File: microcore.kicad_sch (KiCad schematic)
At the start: 5 parts, among them J1 TE_776231-1, J8 USB_B_Mini, M1 Module:mega-mcu100/0.3, M2 Module-power_12and5V-0.3, M3 Module-vr-max9924-0.3

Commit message: Fix top schematic wiring so labels connect to Hellen module pins
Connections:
- net AN1: now also J1.19, M1.S9 (IN_AUX1_(PB0))
- net AN2: now also J1.21, M1.S8 (IN_AUX2_(PC4/PE9))
- net CAN_H: now also J1.2, M1.W11 (CANH)
- net CAN_L: now also J1.3, M1.W12 (CANL)
- net CLT: now also J1.24 (16), M1.S21 (IN_CLT_(PC2))
- net GND: now also J1.22, J1.23, J8.5 (GND), J8.6 (Shield), M1.G (GND), M2.S1 (GND), M3.G (GND)
- net HALL_CAM: now also J1.27 (17), M1.S16 (IN_CAM_(PA6))
- net IAT: now also J1.25 (17), M1.S20 (IN_IAT_(PC3))
- net IGN1: now also J1.12
- net IGN2: now also J1.13, M1.W9 (IGN2_(PE5))
- net IGN3: now also J1.14, M1.W8 (IGN3_(PE4))
- net IGN4: now also J1.15, M1.W7 (IGN4_(PE3))
- net INJ1: now also J1.4
- net INJ2: now also J1.5
- net INJ3: now also J1.6
- net INJ4: now also J1.7
- net LS1_FP: now also J1.8
- net LS2_IDLE: now also J1.9
- net LS3_BOOST: now also J1.10
- net MAP: now also J1.18, M1.S13 (IN_MAP1_(PC0))
- net OUT_INJ1: now also M1.E17 (OUT_INJ1_(PD3))
- net OUT_INJ2: now also M1.E16 (OUT_INJ2_(PA9))
- net OUT_INJ3: now also M1.E15 (OUT_INJ3_(PD11))
- net OUT_INJ4: now also M1.E14 (OUT_INJ4_(PD10))
- net OUT_LS1: now also M1.E18 (OUT_PWM1_(PD13))
- net OUT_LS2: now also M1.E19 (OUT_PWM2_(PC6))
- net OUT_LS3: now also M1.E20 (OUT_PWM3_(PC7))
- net SGND: now also J1.20, M1.E2 (GNDA), M1.W1 (GNDA)
- net TPS: now also J1.17, M1.S18 (IN_TPS_(PA4))
- net USBID_(PA10): now also J8.4 (ID), M1.N4 (USBID_(PA10)); no longer J8.1 (VBUS)
- net USBM_(PA11): now also J8.2 (D-), M1.N2 (USBM_(PA11))
- net USBP_(PA12): now also M1.N3 (USBP_(PA12))
- net V12_RAW: now also M2.V3 (V12_RAW)
- net V5_REF: now also J1.16, M2.E4 (V5), M3.E4 (V5_IN)
- net VBAT: now also M1.N17 (VBAT), M2.E1 (VBAT)
- net VBUS: now also J8.1 (VBUS), M1.N1 (VBUS); no longer J8.4 (ID)
- net VIGN: now also M2.E3 (VIGN)
- net VIGN_SENSE: now also M1.E5 (IN_VIGN_(PA5)), M2.V2 (IN_VIGN)
- net VR_N: now also J1.29 (17), M3.W1 (VR-/HALL)
- net VR_OUT: now also M1.S14 (IN_CRANK_(PB1)), M3.E3 (OUT)
- net VR_P: now also J1.28 (16), M3.W2 (VR+)
- no-connect marks 0 -> 8
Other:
- moved on the sheet: J8

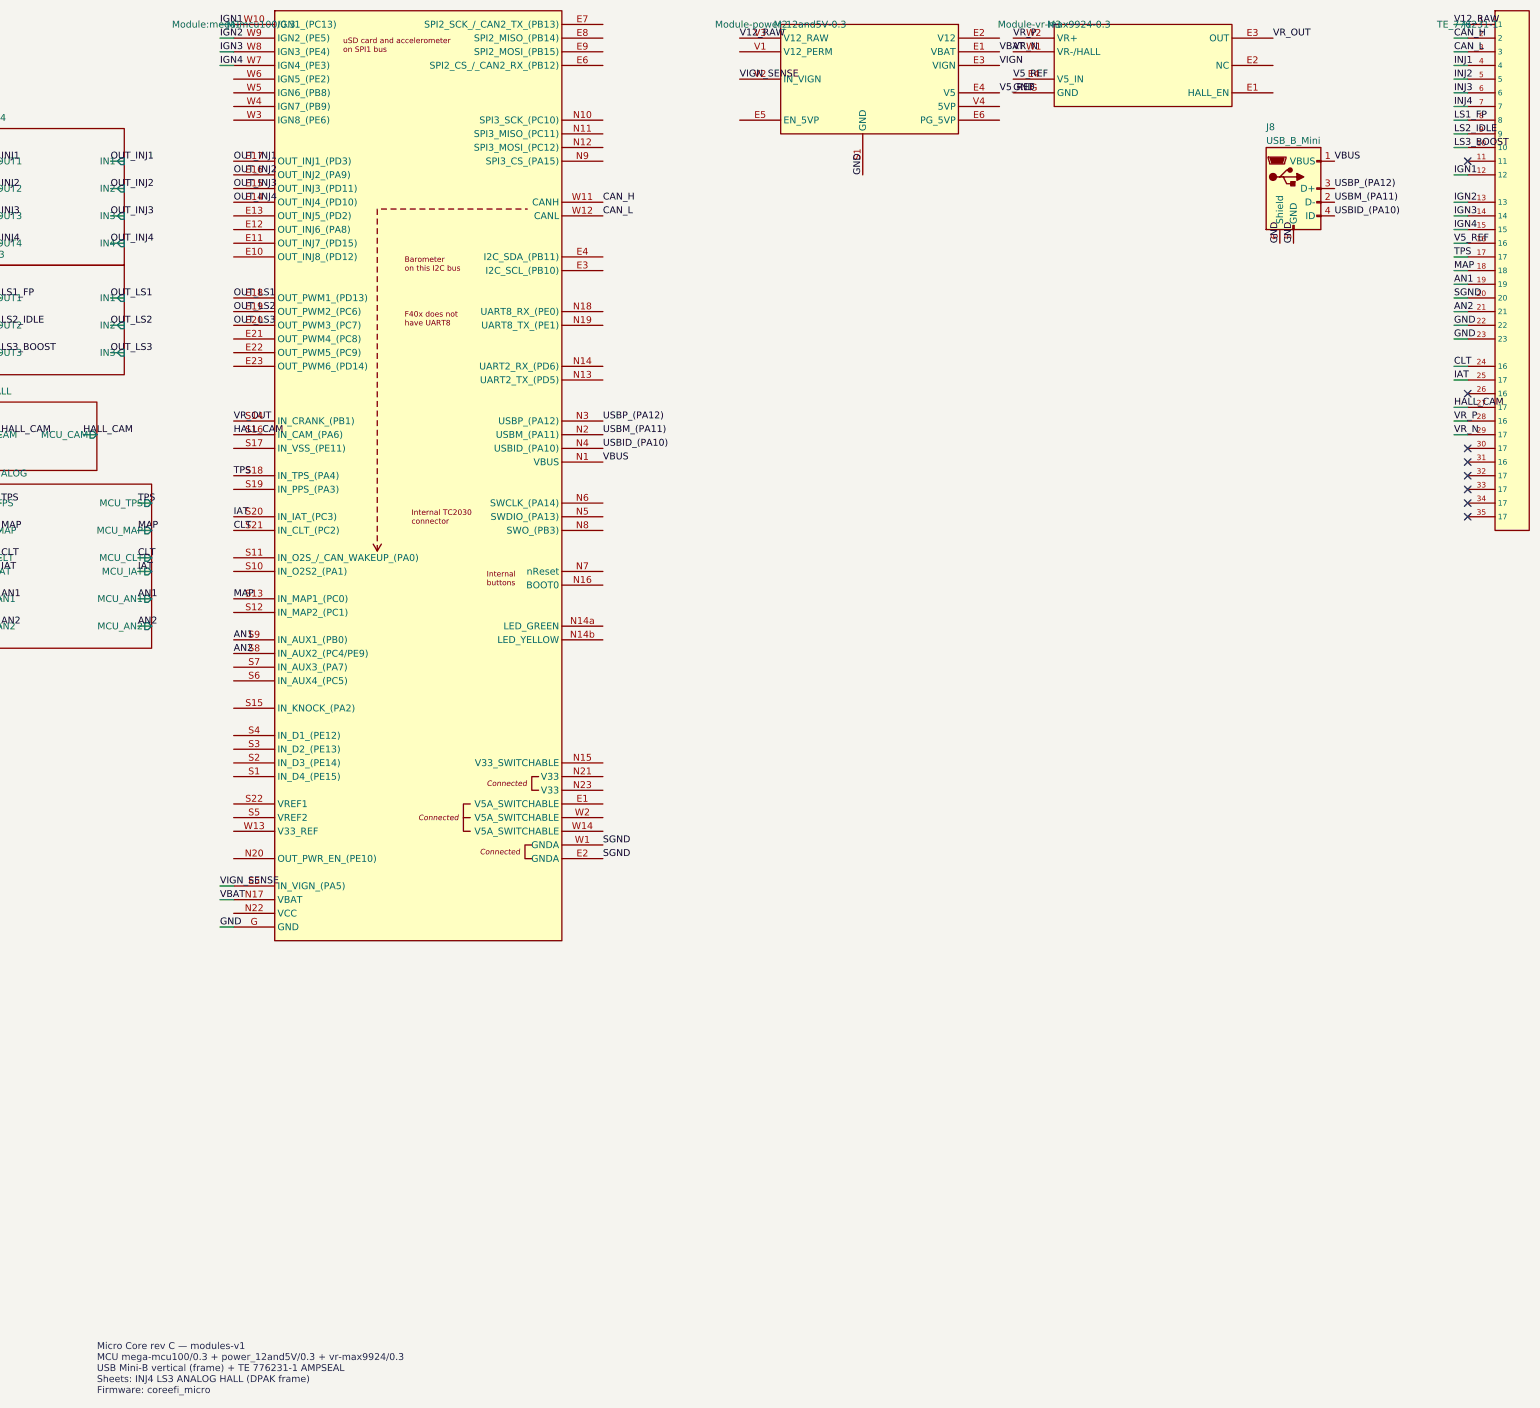
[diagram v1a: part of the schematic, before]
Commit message: Freeze AMPSEAL spare pins and add frame BOOT/RESET (rev d)
Assign pins 11/26/30–35 to DIN1–2, IGN5–8, SGND, PGND; wire to mega.
Add gasketed SW_BOOT (BOOT0–V33) and SW_RESET (nReset–GND) near USB.
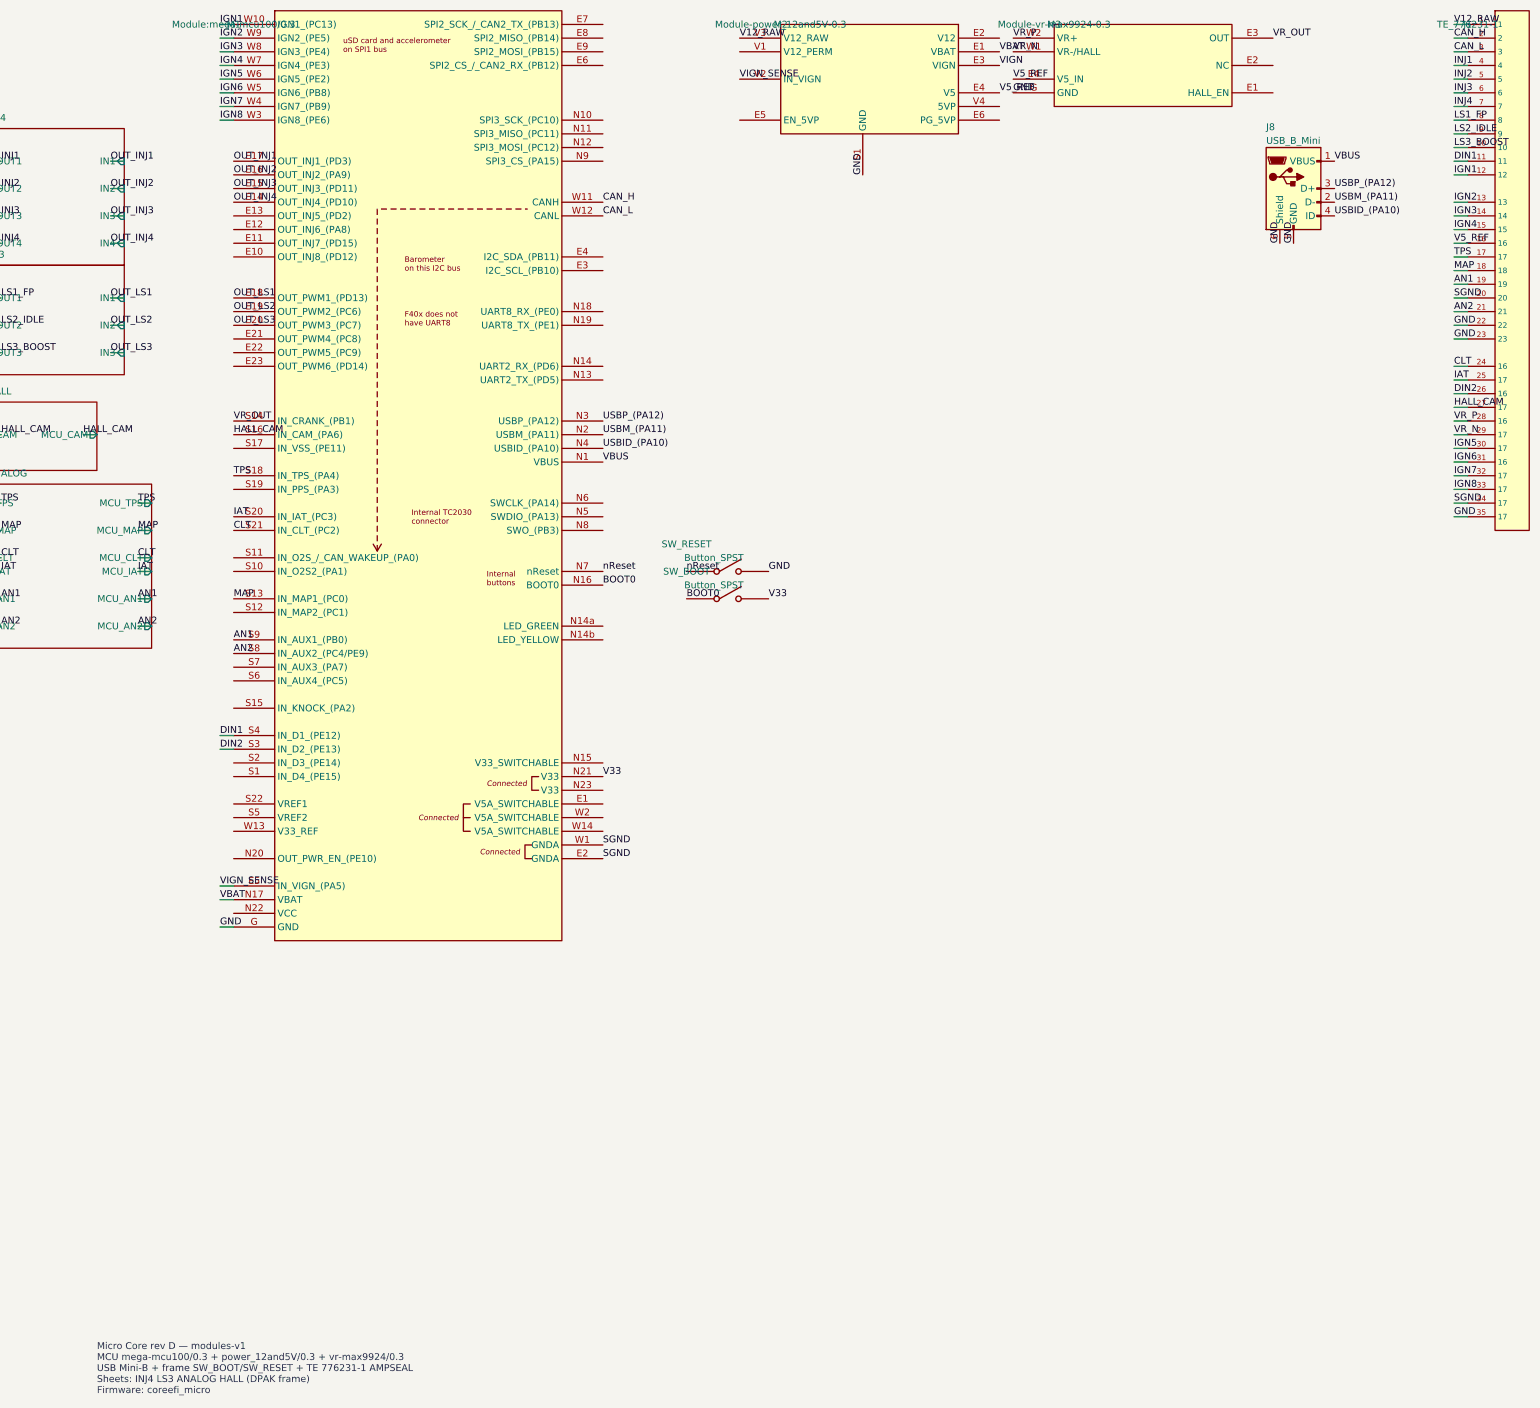
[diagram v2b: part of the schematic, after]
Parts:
- added SW_BOOT, SW_RESET: Button_SPST, hellen-one-common:SMD-2_2.9x3.9x1.7, symbol hellen-one-common:Button_SPST
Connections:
- net GND: now also J1.35 (17), SW_RESET.2
- net SGND: now also J1.34 (17)
- net BOOT0: now reaches M1.N16 (BOOT0)
- net BOOT0: now also SW_BOOT.1
- net V33: now reaches M1.N21 (V33)
- net V33: now also SW_BOOT.2
- net nReset: now reaches M1.N7 (nReset)
- net nReset: now also SW_RESET.1
- net DIN2: now reaches M1.S3 (IN_D2_(PE13))
- net DIN2: now also J1.26 (16)
- net DIN1: now reaches M1.S4 (IN_D1_(PE12))
- net DIN1: now also J1.11
- net IGN8: now reaches M1.W3 (IGN8_(PE6))
- net IGN8: now also J1.33 (17)
- net IGN7: now reaches M1.W4 (IGN7_(PB9))
- net IGN7: now also J1.32 (17)
- net IGN6: now reaches M1.W5 (IGN6_(PB8))
- net IGN6: now also J1.31 (16)
- net IGN5: now reaches M1.W6 (IGN5_(PE2))
- net IGN5: now also J1.30 (17)
- no-connect marks 8 -> 0
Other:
- note added: "Micro Core rev D — modules-v1 MCU mega-mcu100/0.3 + power_12and5V/0.3 + vr-max9924/0.3 USB Mini-B + frame SW_BOOT/SW_RESET + TE 776231-1 AMPSEAL Sheets: INJ4 LS3 ANALOG HALL (DPAK frame) Firmware: coreefi_micro"
- note removed: "Micro Core rev C — modules-v1 MCU mega-mcu100/0.3 + power_12and5V/0.3 + vr-max9924/0.3 USB Mini-B vertical (frame) + TE 776231-1 AMPSEAL Sheets: INJ4 LS3 ANALOG HALL (DPAK frame) Firmware: coreefi_micro"

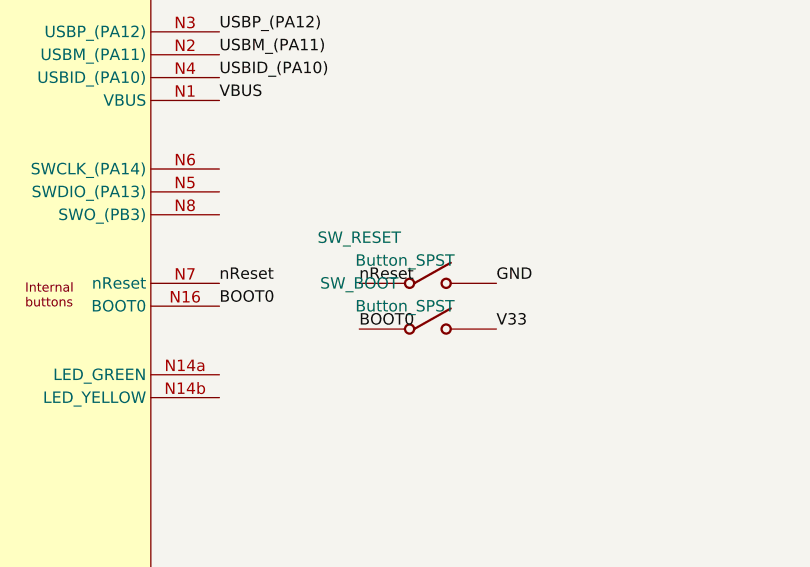
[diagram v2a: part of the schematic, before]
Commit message: Align frame button BOM comment with mega BTN (C115357)
Create Board failed: Comment mismatch for C115357 Button_SPST vs BTN.
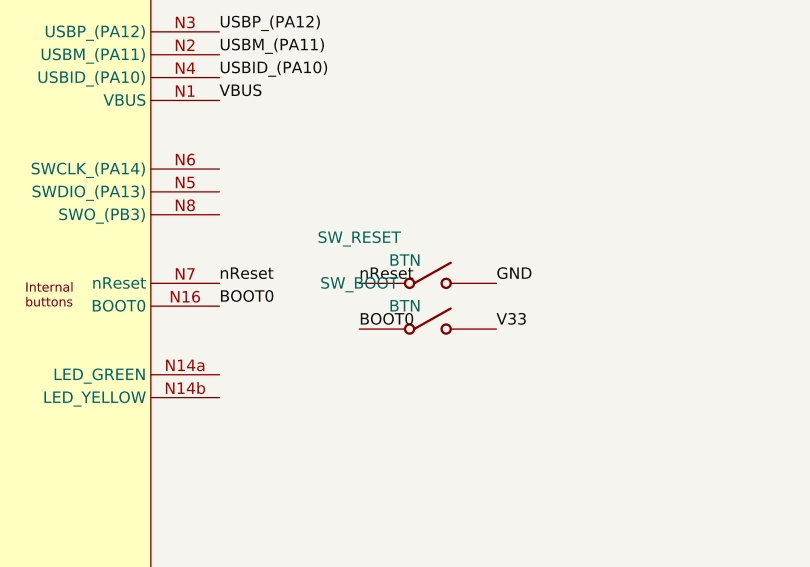
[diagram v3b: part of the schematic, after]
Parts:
- SW_BOOT, SW_RESET: value Button_SPST -> BTN
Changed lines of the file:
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@@
 			)
 		)
-		(property "Value" "Button_SPST"
+		(property "Value" "BTN"
 			(at 140 129.54 0)
 			(effects
@@
 			)
 		)
-		(property "Value" "Button_SPST"
+		(property "Value" "BTN"
 			(at 140 124.46 0)
 			(effects
